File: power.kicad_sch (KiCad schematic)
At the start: 28 parts, among them J2 BAT1_XT60, U3 INA180A2IDBVT, U4 TPS54336ADDA, U5 AMS1117

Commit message: power sch. done, MCU powering as well
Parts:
- removed C1: C, Capacitor_THT:C_Radial_D12.5mm_H25.0mm_P5.00mm, symbol Device:C
- removed R5: 143k, RES_L500x_BRN:RES_L500x_BRN, symbol Device:R
- removed U5: AMS1117, Package_TO_SOT_SMD:SOT-223-3_TabPin2, symbol Regulator_Linear:AMS1117
- added C18: 0.01u, Capacitor_THT:C_Radial_D12.5mm_H25.0mm_P5.00mm, symbol Device:C
- added U6: AMS1117-3.3, Package_TO_SOT_SMD:SOT-223-3_TabPin2, symbol Regulator_Linear:AMS1117-3.3
- C2: value C -> 0.1u
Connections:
- net VSS is gone; now on net +3.3V_OUT: C2.2, U3.5 (VS)
- net +3.3V_OUT: now also U6.2 (VO)
- net +5V_OUT: now also U6.3 (VI)
- net GND: now also C18.2, U6.1 (GND)
- net at U4.8 (SS): now also C18.1

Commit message: Small ammendments
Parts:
- added C22: 100n, symbol Device:C
- added R15: 100k, symbol Device:R
- added R16: 11k, symbol Device:R
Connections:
- net ADC_C_SENSE: now also R2.2; no longer R2.1
- net GND: now also J2.2 (Pin_2), C22.2, R16.2; no longer J2.1 (Pin_1)
- net at C5.1, C6.1, R4.2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: now also R1.1; no longer R1.2
- net at U3.1 (OUT): now also R2.1; no longer R2.2
- new net ADC_V_SENSE: C22.1, R15.2, R16.1
- new net VBAT+: J2.1 (Pin_1), R1.2, R15.1, U3.3 (IN+)
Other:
- moved on the sheet: C12, C13, C14, C15, C2, C3, J2, R1, R2, U3, U6

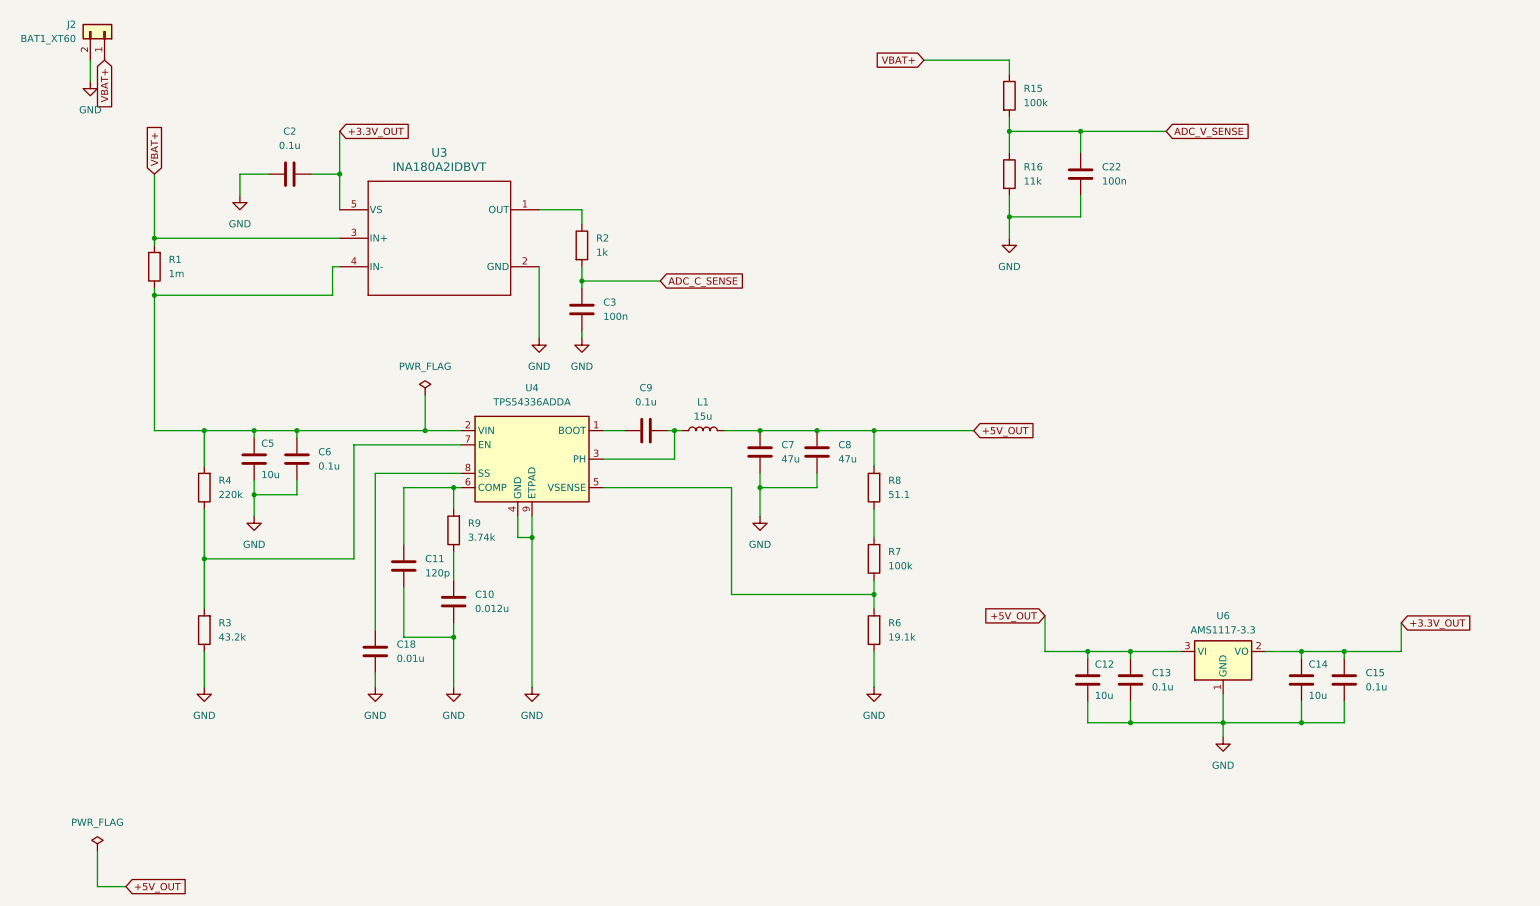
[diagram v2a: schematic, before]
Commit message: ESCs connectors and proper current sensing implemented
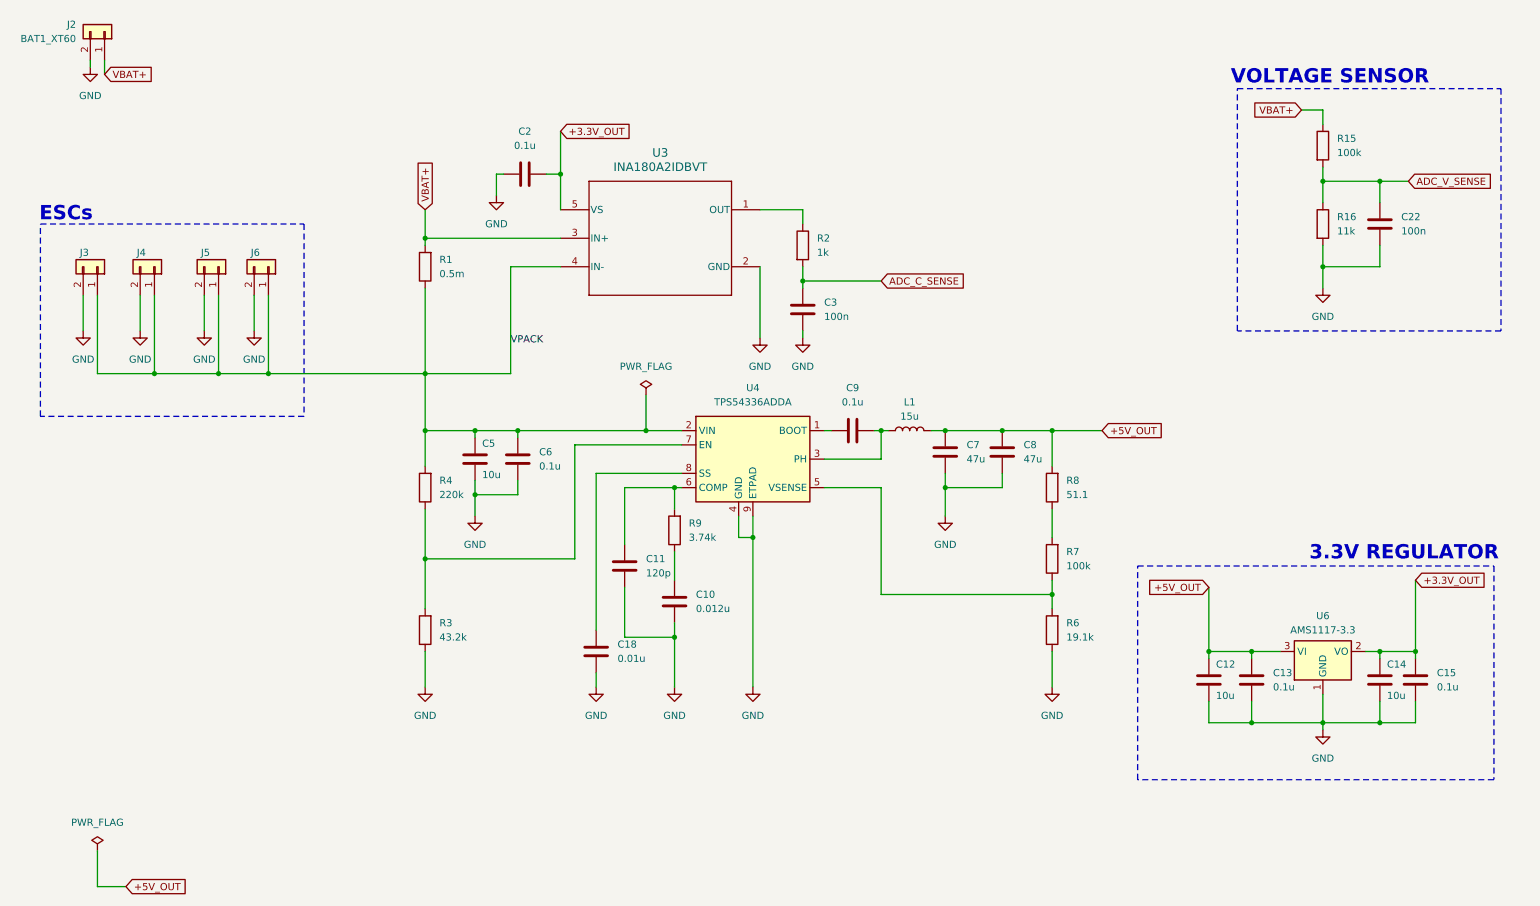
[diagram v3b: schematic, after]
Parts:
- added J3, J4, J5, J6: Conn_01x02, symbol Connector_Generic:Conn_01x02
- R1: value 1m -> 0.5m
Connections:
- net GND: now also J3.2 (Pin_2), J4.2 (Pin_2), J5.2 (Pin_2), J6.2 (Pin_2)
- net VPACK: now reaches C5.1, C6.1, R1.1, R4.2, U3.4 (IN-), U4.2 (VIN)
- net VPACK: now also J3.1 (Pin_1), J4.1 (Pin_1), J5.1 (Pin_1), J6.1 (Pin_1)
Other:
- note added: "3.3V REGULATOR"
- note added: "ESCs"
- note added: "VOLTAGE SENSOR"
- moved on the sheet: C10, C11, C12, C13, C14, C15, C18, C2, C22, C3, C5, C6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

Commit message: 8.09.2026 - 18:56
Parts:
- added C23, C24: 470u, Capacitor_THT:CP_Radial_D10.0mm_P5.00mm, symbol Device:C
- added C25, C26, C27, C28: 4.7u, Capacitor_SMD:C_1206_3216Metric_Pad1.33x1.80mm_HandSolder, symbol Device:C
- J3, J4, J5, J6: footprint (none) -> Connector_AMASS:AMASS_XT30PW-F_1x02_P2.50mm_Horizontal
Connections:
- net GND: now also C23.1, C24.1, C25.1, C26.1, C27.1, C28.1
- net VPACK: now also C23.2, C24.2, C25.2, C26.2, C27.2, C28.2
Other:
- moved on the sheet: C10, C11, C12, C13, C14, C15, C18, C2, C22, C3, C5, C6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

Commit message: 8.09.2026 - 19:33
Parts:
- C23, C24: value 470u -> 470u 50V
- C25, C26, C27, C28: value 4.7u -> 4.7u 50V
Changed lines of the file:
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@@
 	(wire
 		(pts
-			(xy 26.67 55.88) (xy 26.67 73.66)
+			(xy 26.67 55.88) (xy 26.67 72.39)
 		)
 		(stroke
@@
 	(wire
 		(pts
-			(xy 58.42 55.88) (xy 58.42 73.66)
+			(xy 58.42 55.88) (xy 58.42 72.39)
 		)
 		(stroke
@@
 	(wire
 		(pts
-			(xy 43.18 55.88) (xy 43.18 73.66)
+			(xy 43.18 55.88) (xy 43.18 72.39)
 		)
 		(stroke
@@
 	(symbol
 		(lib_id "power:GND")
-		(at 26.67 73.66 0)
+		(at 26.67 72.39 0)
 		(unit 1)
 		(body_style 1)
@@
 		(fields_autoplaced yes)
 		(property "Reference" "#PWR024"
-			(at 26.67 80.01 0)
+			(at 26.67 78.74 0)
 			(hide yes)
 			(show_name no)
@@
 		)
 		(property "Value" "GND"
-			(at 26.67 78.74 0)
+			(at 26.67 77.47 0)
 			(show_name no)
 			(do_not_autoplace no)
@@
 		)
 		(property "Footprint" ""
-			(at 26.67 73.66 0)
+			(at 26.67 72.39 0)
 			(hide yes)
 			(show_name no)
@@
 		)
 		(property "Datasheet" ""
-			(at 26.67 73.66 0)
+			(at 26.67 72.39 0)
 			(hide yes)
 			(show_name no)
@@
 		)
 		(property "Description" "Power symbol creates a global label with name \"GND\" , ground"
-			(at 26.67 73.66 0)
+			(at 26.67 72.39 0)
 			(hide yes)
 			(show_name no)
@@
 	(symbol
 		(lib_id "power:GND")
-		(at 43.18 73.66 0)
+		(at 43.18 72.39 0)
 		(unit 1)
 		(body_style 1)
@@
 		(fields_autoplaced yes)
 		(property "Reference" "#PWR025"
-			(at 43.18 80.01 0)
+			(at 43.18 78.74 0)
 			(hide yes)
 			(show_name no)
@@
 		)
 		(property "Value" "GND"
-			(at 43.18 78.74 0)
+			(at 43.18 77.47 0)
 			(show_name no)
 			(do_not_autoplace no)
@@
 		)
 		(property "Footprint" ""
-			(at 43.18 73.66 0)
+			(at 43.18 72.39 0)
 			(hide yes)
 			(show_name no)
@@
 		)
 		(property "Datasheet" ""
-			(at 43.18 73.66 0)
+			(at 43.18 72.39 0)
 			(hide yes)
 			(show_name no)
@@
 		)
 		(property "Description" "Power symbol creates a global label with name \"GND\" , ground"
-			(at 43.18 73.66 0)
+			(at 43.18 72.39 0)
 			(hide yes)
 			(show_name no)
@@
 			)
 		)
-		(property "Value" "470u"
+		(property "Value" "470u 50V"
 			(at 105.41 96.012 0)
+			(hide yes)
 			(show_name no)
 			(do_not_autoplace no)
@@
 			)
 		)
-		(property "Value" "4.7u"
+		(property "Value" "4.7u 50V"
 			(at 53.34 64.7699 0)
+			(hide yes)
 			(show_name no)
 			(do_not_autoplace no)
@@
 			)
 		)
-		(property "Value" "470u"
+		(property "Value" "470u 50V"
 			(at 93.726 96.012 0)
 			(show_name no)
@@
 	(symbol
 		(lib_id "power:GND")
-		(at 58.42 73.66 0)
+		(at 58.42 72.39 0)
 		(unit 1)
 		(body_style 1)
@@
 		(fields_autoplaced yes)
 		(property "Reference" "#PWR026"
-			(at 58.42 80.01 0)
+			(at 58.42 78.74 0)
 			(hide yes)
 			(show_name no)
@@
 		)
 		(property "Value" "GND"
-			(at 58.42 78.74 0)
+			(at 58.42 77.47 0)
 			(show_name no)
 			(do_not_autoplace no)
@@
 		)
 		(property "Footprint" ""
-			(at 58.42 73.66 0)
+			(at 58.42 72.39 0)
 			(hide yes)
 			(show_name no)
@@
 		)
 		(property "Datasheet" ""
-			(at 58.42 73.66 0)
+			(at 58.42 72.39 0)
 			(hide yes)
 			(show_name no)
@@
 		)
 		(property "Description" "Power symbol creates a global label with name \"GND\" , ground"
-			(at 58.42 73.66 0)
+			(at 58.42 72.39 0)
 			(hide yes)
 			(show_name no)
@@
 		(in_pos_files yes)
 		(dnp no)
-		(fields_autoplaced yes)
 		(property "Reference" "C28"
-			(at 36.83 62.2299 0)
+			(at 33.274 61.468 0)
 			(show_name no)
 			(do_not_autoplace no)
@@
 			)
 		)
-		(property "Value" "4.7u"
-			(at 36.83 64.7699 0)
+		(property "Value" "4.7u 50V"
+			(at 33.274 65.786 0)
 			(show_name no)
 			(do_not_autoplace no)
@@
 			)
 		)
-		(property "Value" "4.7u"
+		(property "Value" "4.7u 50V"
 			(at 83.82 64.7699 0)
+			(hide yes)
 			(show_name no)
 			(do_not_autoplace no)
@@
 			)
 		)
-		(property "Value" "4.7u"
+		(property "Value" "4.7u 50V"
 			(at 68.58 64.7699 0)
+			(hide yes)
 			(show_name no)
 			(do_not_autoplace no)

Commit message: 8.09.2026 - 20:26
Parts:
- J2: footprint Connector_AMASS:AMASS_XT60-M_1x02_P7.20mm_Vertical -> Connector_AMASS:AMASS_XT60PW-M_1x02_P7.20mm_Horizontal
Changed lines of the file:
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@@
 			)
 		)
-		(property "Footprint" "Connector_AMASS:AMASS_XT60-M_1x02_P7.20mm_Vertical"
+		(property "Footprint" "Connector_AMASS:AMASS_XT60PW-M_1x02_P7.20mm_Horizontal"
 			(at 30.48 20.32 0)
 			(hide yes)

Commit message: 15.09.2026 - 21:22
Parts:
- C22: footprint (none) -> Capacitor_SMD:C_0603_1608Metric_Pad1.08x0.95mm_HandSolder
- R15, R16: footprint (none) -> Resistor_SMD:R_0201_0603Metric_Pad0.64x0.40mm_HandSolder
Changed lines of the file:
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@@
 			)
 		)
-		(property "Footprint" ""
+		(property "Footprint" "Resistor_SMD:R_0201_0603Metric_Pad0.64x0.40mm_HandSolder"
 			(at 244.602 31.75 90)
 			(hide yes)
@@
 			)
 		)
-		(property "Footprint" ""
+		(property "Footprint" "Capacitor_SMD:C_0603_1608Metric_Pad1.08x0.95mm_HandSolder"
 			(at 257.5052 49.53 0)
 			(hide yes)
@@
 			)
 		)
-		(property "Footprint" ""
+		(property "Footprint" "Resistor_SMD:R_0201_0603Metric_Pad0.64x0.40mm_HandSolder"
 			(at 244.602 45.72 90)
 			(hide yes)

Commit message: 15.09.2026 21:50
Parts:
- C10, C11, C13, C15, C18, C3, C6, C9: footprint Capacitor_THT:C_Radial_D12.5mm_H25.0mm_P5.00mm -> Capacitor_SMD:C_0603_1608Metric_Pad1.08x0.95mm_HandSolder
- C12, C14, C5, C7, C8: footprint Capacitor_THT:C_Radial_D12.5mm_H25.0mm_P5.00mm -> Capacitor_SMD:C_0805_2012Metric_Pad1.18x1.45mm_HandSolder
- C23, C24: footprint Capacitor_THT:CP_Radial_D10.0mm_P5.00mm -> Capacitor_SMD:C_1206_3216Metric_Pad1.33x1.80mm_HandSolder
- R15, R16: footprint Resistor_SMD:R_0201_0603Metric_Pad0.64x0.40mm_HandSolder -> Resistor_SMD:R_0603_1608Metric_Pad0.98x0.95mm_HandSolder
- R3, R4, R6, R7, R8, R9: footprint RES_L500x_BRN:RES_L500x_BRN -> Resistor_SMD:R_0603_1608Metric_Pad0.98x0.95mm_HandSolder
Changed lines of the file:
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@@
 			)
 		)
-		(property "Footprint" "Capacitor_THT:C_Radial_D12.5mm_H25.0mm_P5.00mm"
+		(property "Footprint" "Capacitor_SMD:C_0805_2012Metric_Pad1.18x1.45mm_HandSolder"
 			(at 235.9152 151.13 0)
 			(hide yes)
@@
 			)
 		)
-		(property "Footprint" "Capacitor_THT:C_Radial_D12.5mm_H25.0mm_P5.00mm"
+		(property "Footprint" "Capacitor_SMD:C_0603_1608Metric_Pad1.08x0.95mm_HandSolder"
 			(at 124.1552 100.33 0)
 			(hide yes)
@@
 			)
 		)
-		(property "Footprint" "Capacitor_THT:CP_Radial_D10.0mm_P5.00mm"
+		(property "Footprint" "Capacitor_SMD:C_1206_3216Metric_Pad1.33x1.80mm_HandSolder"
 			(at 101.2952 90.17 0)
 			(hide yes)
@@
 			)
 		)
-		(property "Footprint" "RES_L500x_BRN:RES_L500x_BRN"
+		(property "Footprint" "Resistor_SMD:R_0603_1608Metric_Pad0.98x0.95mm_HandSolder"
 			(at 147.828 109.22 90)
 			(hide yes)
@@
 			)
 		)
-		(property "Footprint" "Capacitor_THT:C_Radial_D12.5mm_H25.0mm_P5.00mm"
+		(property "Footprint" "Capacitor_SMD:C_0805_2012Metric_Pad1.18x1.45mm_HandSolder"
 			(at 194.0052 100.33 0)
 			(hide yes)
@@
 			)
 		)
-		(property "Footprint" "RES_L500x_BRN:RES_L500x_BRN"
+		(property "Footprint" "Resistor_SMD:R_0603_1608Metric_Pad0.98x0.95mm_HandSolder"
 			(at 207.518 107.95 90)
 			(hide yes)
@@
 			)
 		)
-		(property "Footprint" "RES_L500x_BRN:RES_L500x_BRN"
+		(property "Footprint" "Resistor_SMD:R_0603_1608Metric_Pad0.98x0.95mm_HandSolder"
 			(at 207.518 97.79 90)
 			(hide yes)
@@
 			)
 		)
-		(property "Footprint" "Capacitor_THT:C_Radial_D12.5mm_H25.0mm_P5.00mm"
+		(property "Footprint" "Capacitor_SMD:C_0603_1608Metric_Pad1.08x0.95mm_HandSolder"
 			(at 138.1252 119.38 0)
 			(hide yes)
@@
 			)
 		)
-		(property "Footprint" "Capacitor_THT:C_Radial_D12.5mm_H25.0mm_P5.00mm"
+		(property "Footprint" "Capacitor_SMD:C_0603_1608Metric_Pad1.08x0.95mm_HandSolder"
 			(at 242.2652 151.13 0)
 			(hide yes)
@@
 			)
 		)
-		(property "Footprint" "Capacitor_THT:CP_Radial_D10.0mm_P5.00mm"
+		(property "Footprint" "Capacitor_SMD:C_1206_3216Metric_Pad1.33x1.80mm_HandSolder"
 			(at 94.9452 90.17 0)
 			(hide yes)
@@
 			)
 		)
-		(property "Footprint" "Capacitor_THT:C_Radial_D12.5mm_H25.0mm_P5.00mm"
+		(property "Footprint" "Capacitor_SMD:C_0603_1608Metric_Pad1.08x0.95mm_HandSolder"
 			(at 169.8752 73.66 0)
 			(hide yes)
@@
 			)
 		)
-		(property "Footprint" "Resistor_SMD:R_0201_0603Metric_Pad0.64x0.40mm_HandSolder"
+		(property "Footprint" "Resistor_SMD:R_0603_1608Metric_Pad0.98x0.95mm_HandSolder"
 			(at 244.602 31.75 90)
 			(hide yes)
@@
 			)
 		)
-		(property "Footprint" "Capacitor_THT:C_Radial_D12.5mm_H25.0mm_P5.00mm"
+		(property "Footprint" "Capacitor_SMD:C_0603_1608Metric_Pad1.08x0.95mm_HandSolder"
 			(at 267.6652 151.13 0)
 			(hide yes)
@@
 			)
 		)
-		(property "Footprint" "RES_L500x_BRN:RES_L500x_BRN"
+		(property "Footprint" "Resistor_SMD:R_0603_1608Metric_Pad0.98x0.95mm_HandSolder"
 			(at 110.998 101.6 90)
 			(hide yes)
@@
 			)
 		)
-		(property "Footprint" "Capacitor_THT:C_Radial_D12.5mm_H25.0mm_P5.00mm"
+		(property "Footprint" "Capacitor_SMD:C_0805_2012Metric_Pad1.18x1.45mm_HandSolder"
 			(at 200.3552 100.33 0)
 			(hide yes)
@@
 			)
 		)
-		(property "Footprint" "Capacitor_THT:C_Radial_D12.5mm_H25.0mm_P5.00mm"
+		(property "Footprint" "Capacitor_SMD:C_0805_2012Metric_Pad1.18x1.45mm_HandSolder"
 			(at 116.5352 100.33 0)
 			(hide yes)
@@
 			)
 		)
-		(property "Footprint" "Capacitor_THT:C_Radial_D12.5mm_H25.0mm_P5.00mm"
+		(property "Footprint" "Capacitor_SMD:C_0603_1608Metric_Pad1.08x0.95mm_HandSolder"
 			(at 181.61 90.4748 0)
 			(hide yes)
@@
 			)
 		)
-		(property "Footprint" "Capacitor_THT:C_Radial_D12.5mm_H25.0mm_P5.00mm"
+		(property "Footprint" "Capacitor_SMD:C_0603_1608Metric_Pad1.08x0.95mm_HandSolder"
 			(at 133.0452 134.62 0)
 			(hide yes)
@@
 			)
 		)
-		(property "Footprint" "Capacitor_THT:C_Radial_D12.5mm_H25.0mm_P5.00mm"
+		(property "Footprint" "Capacitor_SMD:C_0805_2012Metric_Pad1.18x1.45mm_HandSolder"
 			(at 261.3152 151.13 0)
 			(hide yes)
@@
 			)
 		)
-		(property "Footprint" "Capacitor_THT:C_Radial_D12.5mm_H25.0mm_P5.00mm"
+		(property "Footprint" "Capacitor_SMD:C_0603_1608Metric_Pad1.08x0.95mm_HandSolder"
 			(at 147.0152 125.73 0)
 			(hide yes)
@@
 			)
 		)
-		(property "Footprint" "RES_L500x_BRN:RES_L500x_BRN"
+		(property "Footprint" "Resistor_SMD:R_0603_1608Metric_Pad0.98x0.95mm_HandSolder"
 			(at 110.998 128.27 90)
 			(hide yes)
@@
 			)
 		)
-		(property "Footprint" "Resistor_SMD:R_0201_0603Metric_Pad0.64x0.40mm_HandSolder"
+		(property "Footprint" "Resistor_SMD:R_0603_1608Metric_Pad0.98x0.95mm_HandSolder"
 			(at 244.602 45.72 90)
 			(hide yes)
@@
 			)
 		)
-		(property "Footprint" "RES_L500x_BRN:RES_L500x_BRN"
+		(property "Footprint" "Resistor_SMD:R_0603_1608Metric_Pad0.98x0.95mm_HandSolder"
 			(at 207.518 118.11 90)
 			(hide yes)
